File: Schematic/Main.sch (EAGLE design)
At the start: 54 parts, among them IC1 PIC18F4550_40, IC2 7805, IC4 AD7734, IC5 AD780, K1 SRD-24VDC-SL-C, K2 SRD-24VDC-SL-C, Q1 20MHz, Q2 6.144MHz, T1 2N2222, U1 LM317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

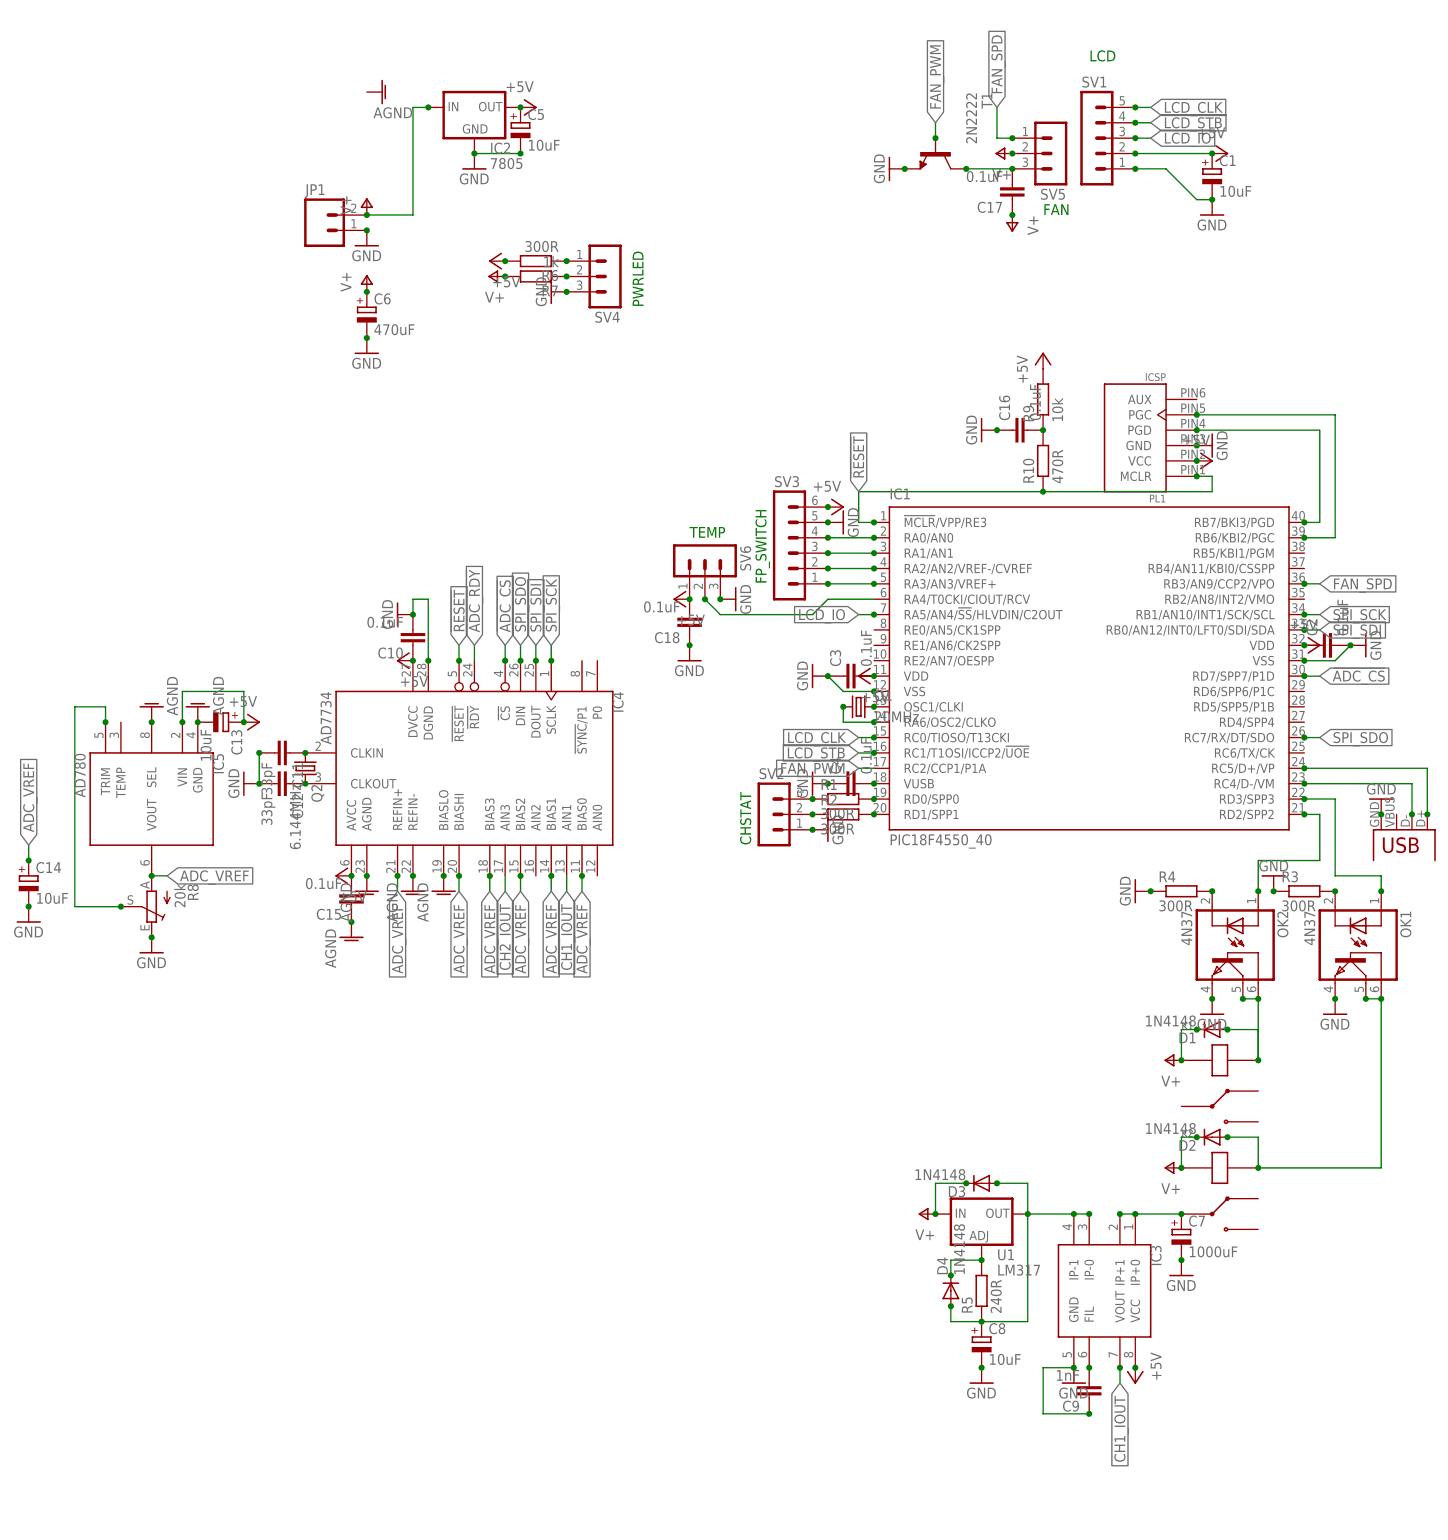
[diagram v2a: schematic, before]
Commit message: Output components use a different gnd from input now.
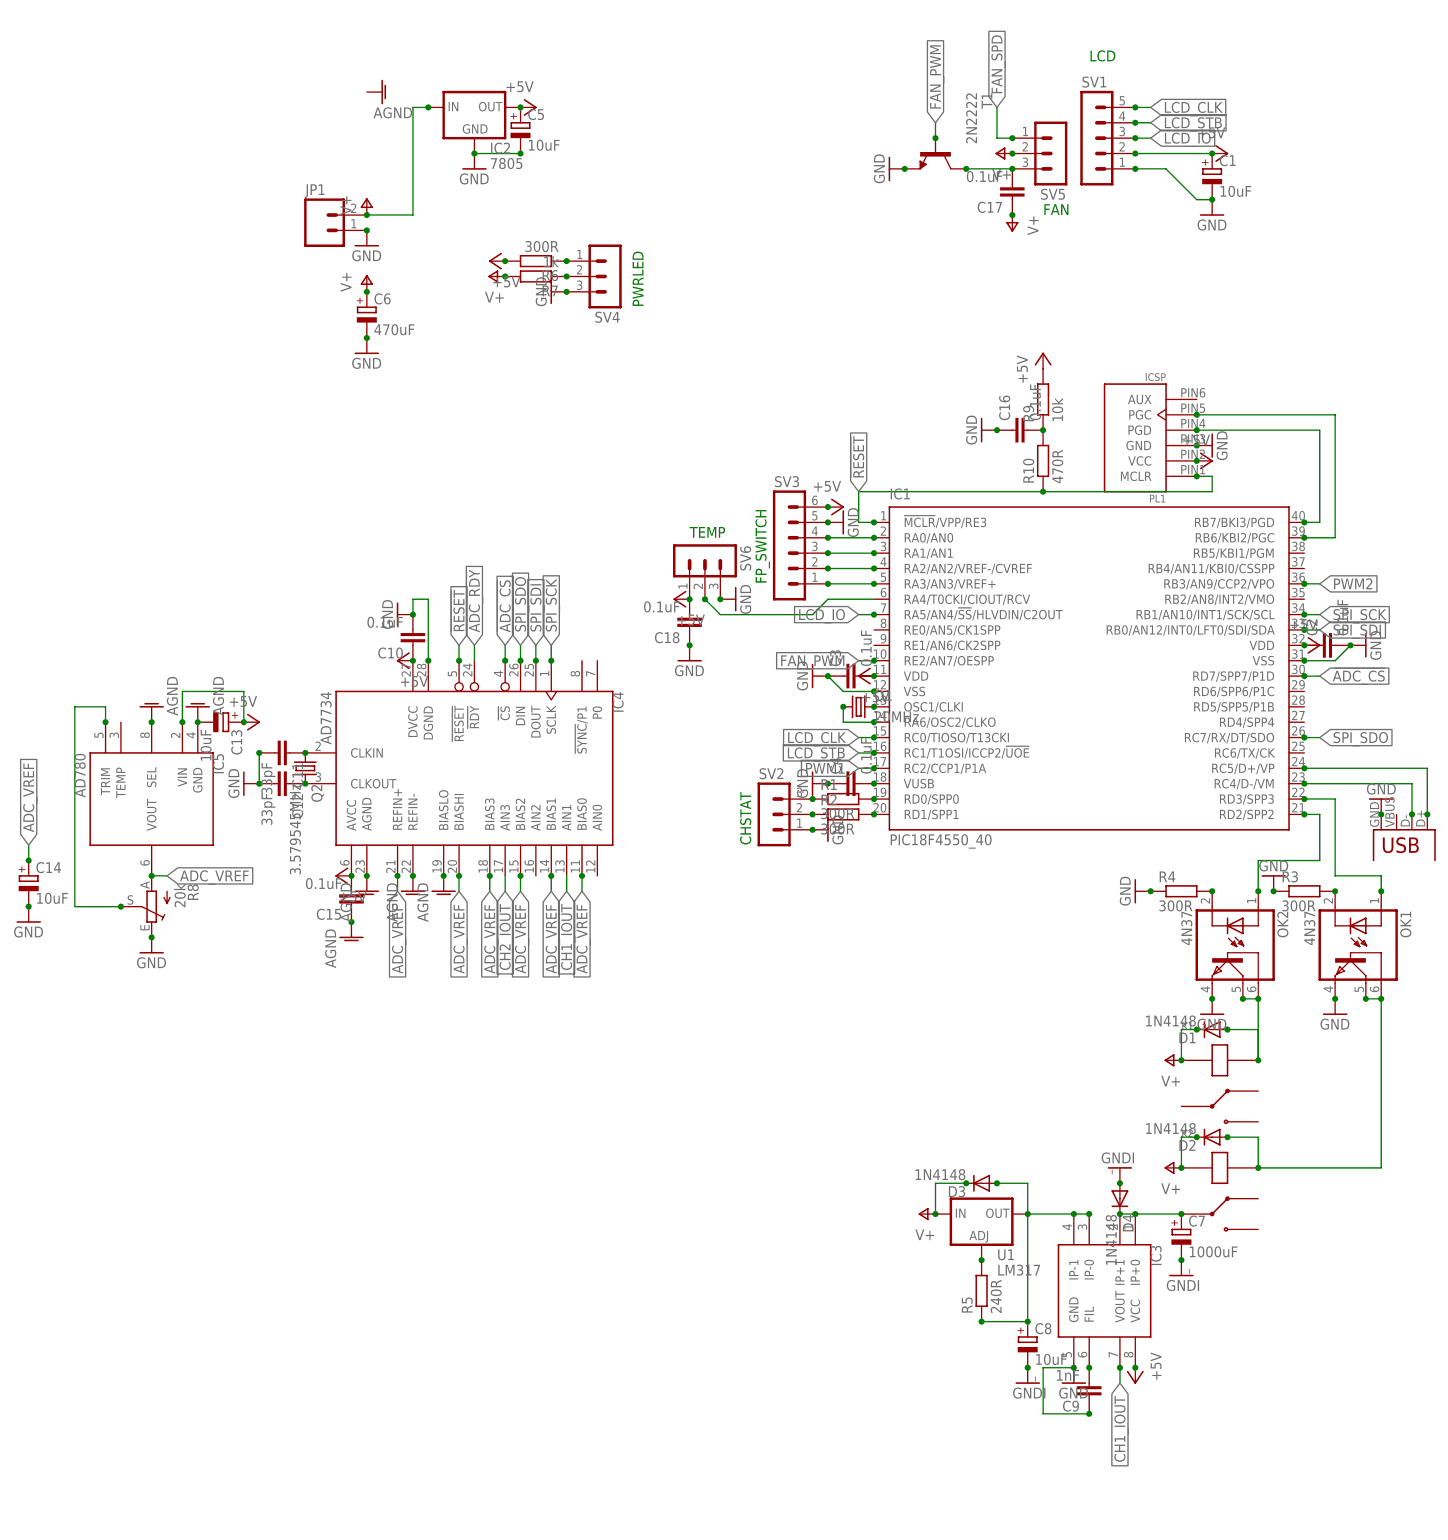
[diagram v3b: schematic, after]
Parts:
- Q2: value 6.144MHz -> 3.579545MHz
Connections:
- new net GNDI: C7.-, C8.-, D4.A
- new net PWM1: IC1.RC2/CCP1/P1A
- new net PWM2: IC1.RB3/AN9/CCP2/VPO
- net FAN_PWM: now also IC1.RE2/AN7/OESPP; no longer IC1.RC2/CCP1/P1A
- net FAN_SPD: no longer IC1.RB3/AN9/CCP2/VPO
- net GND: no longer C7.-, C8.-
- net N$23: no longer D4.C
- net N$26: no longer D4.A
- net N$28: now also D4.C
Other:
- moved on the sheet: C8, D4
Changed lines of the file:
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@@
 <part name="R5" library="rcl" deviceset="R-EU_" device="0204/7" value="240R"/>
 <part name="C7" library="rcl" deviceset="CPOL-EU" device="E5-13" value="1000uF"/>
-<part name="GND16" library="supply1" deviceset="GND" device=""/>
 <part name="D3" library="diode" deviceset="1N4148" device="DO35-7" value="1N4148"/>
-<part name="D4" library="diode" deviceset="1N4148" device="DO35-7" value="1N4148"/>
 <part name="C8" library="rcl" deviceset="CPOL-EU" device="E2.5-5" value="10uF"/>
-<part name="GND17" library="supply1" deviceset="GND" device=""/>
 <part name="P+11" library="supply1" deviceset="V+" device=""/>
 <part name="R6" library="rcl" deviceset="R-EU_" device="0204/7" value="300R"/>
@@
 <part name="GND21" library="supply1" deviceset="GND" device=""/>
 <part name="P+16" library="supply1" deviceset="+5V" device=""/>
-<part name="Q2" library="crystal" deviceset="CRYSTAL" device="HC49S" value="6.144MHz"/>
+<part name="Q2" library="crystal" deviceset="CRYSTAL" device="HC49S" value="3.579545MHz"/>
 <part name="C11" library="rcl" deviceset="C-EU" device="025-030X050" value="33pF"/>
 <part name="C12" library="rcl" deviceset="C-EU" device="025-030X050" value="33pF"/>
@@
 <part name="C18" library="rcl" deviceset="C-EU" device="025-030X050" value="0.1uF"/>
 <part name="GND27" library="supply1" deviceset="GND" device=""/>
+<part name="GNDI1" library="supply1" deviceset="GNDI" device=""/>
+<part name="GNDI2" library="supply1" deviceset="GNDI" device=""/>
+<part name="D4" library="diode" deviceset="1N4148" device="DO35-7" value="1N4148"/>
+<part name="GNDI4" library="supply1" deviceset="GNDI" device=""/>
 </parts>
 <sheets>
@@
 <instance part="R5" gate="G$1" x="-17.78" y="-101.6" rot="R90"/>
 <instance part="C7" gate="G$1" x="15.24" y="-91.44"/>
-<instance part="GND16" gate="1" x="15.24" y="-99.06"/>
 <instance part="D3" gate="G$1" x="-17.78" y="-83.82" rot="R180"/>
-<instance part="D4" gate="G$1" x="-22.86" y="-101.6" rot="R90"/>
-<instance part="C8" gate="G$1" x="-17.78" y="-109.22"/>
-<instance part="GND17" gate="1" x="-17.78" y="-116.84"/>
+<instance part="C8" gate="G$1" x="-10.16" y="-109.22"/>
 <instance part="P+11" gate="1" x="-27.94" y="-88.9" rot="R90"/>
 <instance part="R6" gate="G$1" x="-91.44" y="68.58" rot="R180"/>
@@
 <instance part="C18" gate="G$1" x="-66.04" y="7.62" rot="R180"/>
 <instance part="GND27" gate="1" x="-66.04" y="2.54"/>
+<instance part="GNDI1" gate="G$1" x="-10.16" y="-116.84"/>
+<instance part="GNDI2" gate="G$1" x="15.24" y="-99.06"/>
+<instance part="D4" gate="G$1" x="5.08" y="-86.36" rot="R270"/>
+<instance part="GNDI4" gate="G$1" x="5.08" y="-81.28" rot="R180"/>
 </instances>
 <busses>
@@
 <pinref part="GND15" gate="1" pin="GND"/>
 <junction x="40.64" y="-53.34"/>
-</segment>
-<segment>
-<pinref part="C7" gate="G$1" pin="-"/>
-<pinref part="GND16" gate="1" pin="GND"/>
-<junction x="15.24" y="-96.52"/>
-</segment>
-<segment>
-<pinref part="C8" gate="G$1" pin="-"/>
-<pinref part="GND17" gate="1" pin="GND"/>
-<junction x="-17.78" y="-114.3"/>
 </segment>
 <segment>
@@
 <pinref part="U1" gate="G$1" pin="OUT"/>
 <pinref part="R5" gate="G$1" pin="1"/>
-<wire x1="-17.78" y1="-106.68" x2="-10.16" y2="-106.68" width="0.1524" layer="91"/>
 <wire x1="-10.16" y1="-106.68" x2="-10.16" y2="-88.9" width="0.1524" layer="91"/>
 <pinref part="D3" gate="G$1" pin="A"/>
@@
 <wire x1="-10.16" y1="-83.82" x2="-10.16" y2="-88.9" width="0.1524" layer="91"/>
 <junction x="-15.24" y="-83.82"/>
-<pinref part="D4" gate="G$1" pin="A"/>
-<wire x1="-22.86" y1="-104.14" x2="-22.86" y2="-106.68" width="0.1524" layer="91"/>
-<wire x1="-22.86" y1="-106.68" x2="-17.78" y2="-106.68" width="0.1524" layer="91"/>
-<junction x="-22.86" y="-104.14"/>
-<junction x="-17.78" y="-106.68"/>
+<junction x="-10.16" y="-106.68"/>
 <pinref part="C8" gate="G$1" pin="+"/>
 <junction x="-10.16" y="-88.9"/>
@@
 <wire x1="-2.54" y1="-88.9" x2="-10.16" y2="-88.9" width="0.1524" layer="91"/>
 <junction x="0" y="-88.9"/>
+<wire x1="-10.16" y1="-106.68" x2="-17.78" y2="-106.68" width="0.1524" layer="91"/>
+<junction x="-17.78" y="-106.68"/>
 </segment>
 </net>
@@
 <pinref part="R5" gate="G$1" pin="2"/>
 <junction x="-17.78" y="-96.52"/>
-<pinref part="D4" gate="G$1" pin="C"/>
-<wire x1="-17.78" y1="-96.52" x2="-22.86" y2="-96.52" width="0.1524" layer="91"/>
-<wire x1="-22.86" y1="-96.52" x2="-22.86" y2="-99.06" width="0.1524" layer="91"/>
-<junction x="-22.86" y="-99.06"/>
 </segment>
 </net>
@@
 </net>
 <net name="FAN_PWM" class="0">
-<segment>
-<pinref part="IC1" gate="G$1" pin="RC2/CCP1/P1A"/>
-<wire x1="-35.56" y1="-15.24" x2="-38.1" y2="-15.24" width="0.1524" layer="91"/>
-<label x="-38.1" y="-15.24" size="1.778" layer="95" rot="R180" xref="yes"/>
-</segment>
 <segment>
 <pinref part="T1" gate="G$1" pin="B"/>
@@
 <label x="-25.4" y="91.44" size="1.778" layer="95" rot="R90" xref="yes"/>
 <junction x="-25.4" y="88.9"/>
+</segment>
+<segment>
+<pinref part="IC1" gate="G$1" pin="RE2/AN7/OESPP"/>
+<wire x1="-35.56" y1="2.54" x2="-38.1" y2="2.54" width="0.1524" layer="91"/>
+<label x="-38.1" y="2.54" size="1.778" layer="95" rot="R180" xref="yes"/>
+<junction x="-35.56" y="2.54"/>
 </segment>
 </net>
@@
 <label x="-15.24" y="93.98" size="1.778" layer="95" rot="R90" xref="yes"/>
 <junction x="-12.7" y="88.9"/>
-</segment>
-<segment>
-<pinref part="IC1" gate="G$1" pin="RB3/AN9/CCP2/VPO"/>
-<wire x1="38.1" y1="15.24" x2="35.56" y2="15.24" width="0.1524" layer="91"/>
-<label x="38.1" y="15.24" size="1.778" layer="95" xref="yes"/>
-<junction x="35.56" y="15.24"/>
 </segment>
 </net>
@@
 <wire x1="7.62" y1="-88.9" x2="15.24" y2="-88.9" width="0.1524" layer="91"/>
 <junction x="15.24" y="-88.9"/>
+<pinref part="D4" gate="G$1" pin="C"/>
 </segment>
 </net>
@@
 </segment>
 </net>
+<net name="GNDI" class="0">
+<segment>
+<pinref part="C8" gate="G$1" pin="-"/>
+<pinref part="GNDI1" gate="G$1" pin="GNDI"/>
+<junction x="-10.16" y="-114.3"/>
+</segment>
+<segment>
+<pinref part="C7" gate="G$1" pin="-"/>
+<pinref part="GNDI2" gate="G$1" pin="GNDI"/>
+<junction x="15.24" y="-96.52"/>
+</segment>
+<segment>
+<pinref part="D4" gate="G$1" pin="A"/>
+<pinref part="GNDI4" gate="G$1" pin="GNDI"/>
+<junction x="5.08" y="-83.82"/>
+</segment>
+</net>
+<net name="PWM2" class="0">
+<segment>
+<pinref part="IC1" gate="G$1" pin="RB3/AN9/CCP2/VPO"/>
+<wire x1="38.1" y1="15.24" x2="35.56" y2="15.24" width="0.1524" layer="91"/>
+<label x="38.1" y="15.24" size="1.778" layer="95" xref="yes"/>
+<junction x="35.56" y="15.24"/>
+</segment>
+</net>
+<net name="PWM1" class="0">
+<segment>
+<pinref part="IC1" gate="G$1" pin="RC2/CCP1/P1A"/>
+<wire x1="-35.56" y1="-15.24" x2="-38.1" y2="-15.24" width="0.1524" layer="91"/>
+<label x="-38.1" y="-15.24" size="1.778" layer="95" rot="R180" xref="yes"/>
+<junction x="-35.56" y="-15.24"/>
+</segment>
+</net>

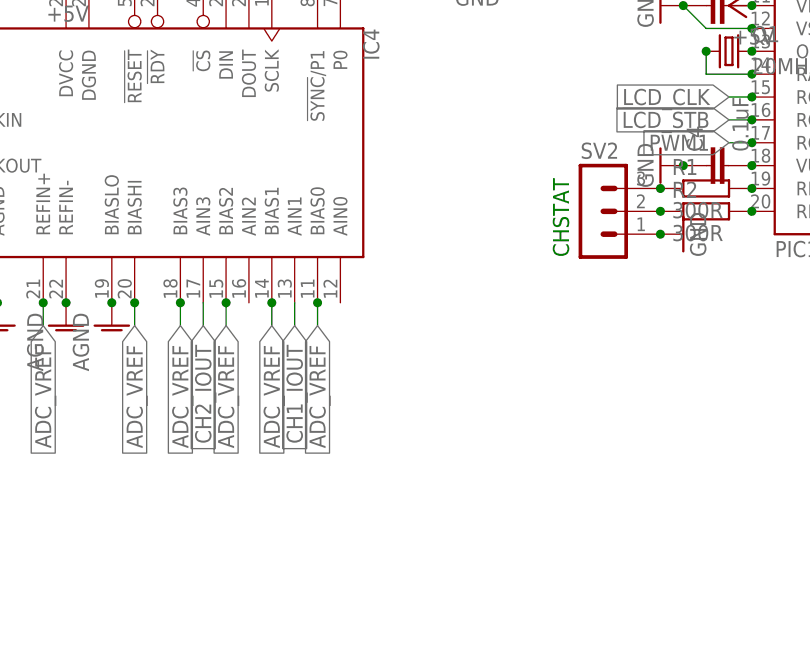
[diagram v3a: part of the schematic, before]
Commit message: Moved some pins around.
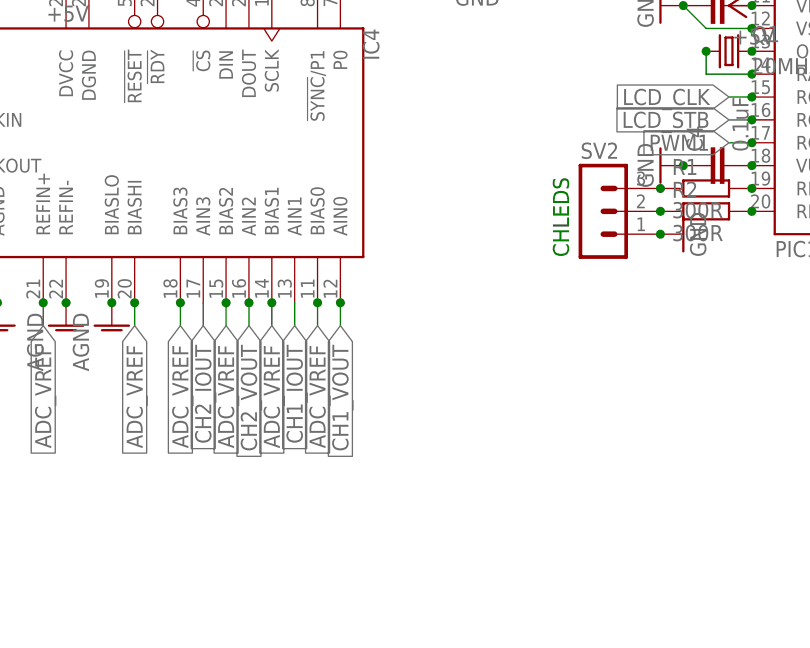
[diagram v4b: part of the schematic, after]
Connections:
- new net CH1_VOUT: IC4.AIN0
- new net CH2_VOUT: IC4.AIN2
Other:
- note added: "CHLEDS"
- note removed: "CHSTAT"
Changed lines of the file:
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@@
 <text x="-53.34" y="15.24" size="1.778" layer="91" rot="R90">FP_SWITCH</text>
 <text x="-66.04" y="22.86" size="1.778" layer="91">TEMP</text>
-<text x="-55.88" y="-27.94" size="1.778" layer="91" rot="R90">CHSTAT</text>
+<text x="-55.88" y="-27.94" size="1.778" layer="91" rot="R90">CHLEDS</text>
 <text x="-7.62" y="76.2" size="1.778" layer="91">FAN</text>
 <text x="0" y="101.6" size="1.778" layer="91">LCD</text>
@@
 </segment>
 </net>
+<net name="CH2_VOUT" class="0">
+<segment>
+<pinref part="IC4" gate="G$1" pin="AIN2"/>
+<wire x1="-91.44" y1="-33.02" x2="-91.44" y2="-35.56" width="0.1524" layer="91"/>
+<label x="-91.44" y="-35.56" size="1.778" layer="95" rot="R270" xref="yes"/>
+<junction x="-91.44" y="-33.02"/>
+</segment>
+</net>
+<net name="CH1_VOUT" class="0">
+<segment>
+<pinref part="IC4" gate="G$1" pin="AIN0"/>
+<wire x1="-81.28" y1="-33.02" x2="-81.28" y2="-35.56" width="0.1524" layer="91"/>
+<label x="-81.28" y="-35.56" size="1.778" layer="95" rot="R270" xref="yes"/>
+<junction x="-81.28" y="-33.02"/>
+</segment>
+</net>
